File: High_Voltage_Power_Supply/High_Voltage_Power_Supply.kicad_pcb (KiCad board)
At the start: 2 copper layers, 170 x 100 mm, 64 parts, among them J1 Conn_01x02_Female, J2 Conn_01x02_Female, J3 Conn_01x02_Female, J4 Conn_01x12_Female, Q1 Q_NMOS_GDS, Q2 Q_NMOS_GDS, Q3 Q_NIGBT_GCE, U1 LT3751-TSSOP, U2 LT3751-TSSOP, U3 MC14504B, U4 MC14504B, U5 ADCMP356, U6 ZXGD3004E6

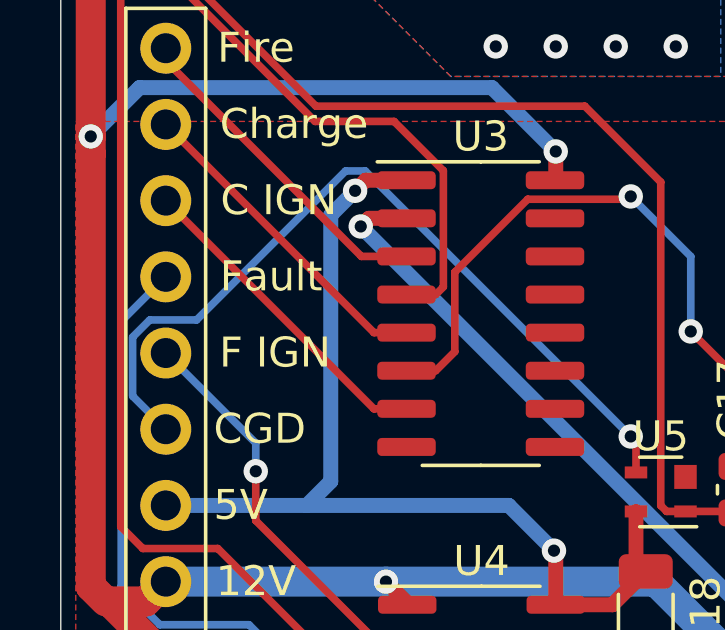
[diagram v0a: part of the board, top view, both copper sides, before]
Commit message: pin labling error fixed and arduino project for testing added
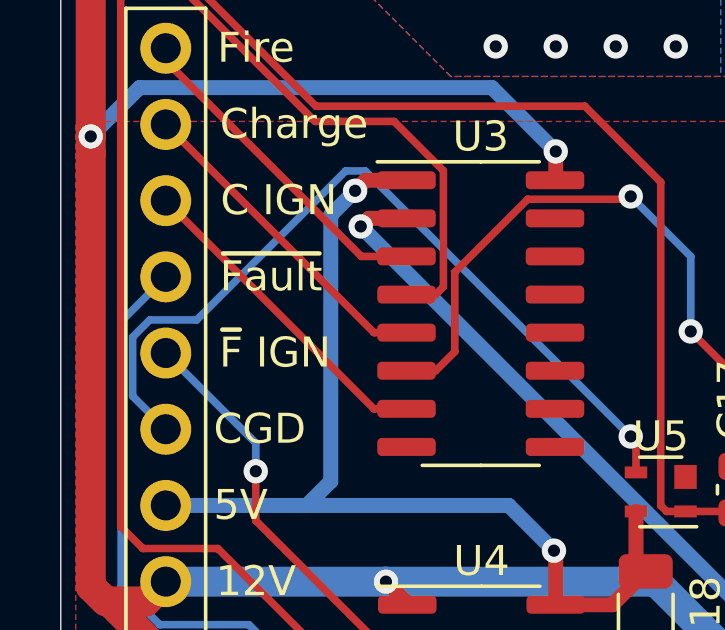
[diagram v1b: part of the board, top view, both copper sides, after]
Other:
- board text added: "~F IGN~"
- board text added: "~Fault~"
- board text removed: "F IGN"
- board text removed: "Fault"

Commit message: Created V3 of the schematic
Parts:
- added C19: 5uF, Capacitor_THT:C_Rect_L31.5mm_W20.0mm_P27.50mm_MKS4, F.Cu at (180.0, 130.0)
- added C20: 100uF, Capacitor_THT:CP_Radial_D8.0mm_P5.00mm, F.Cu at (70.0, 90.0)
- added C21: 100uF, Capacitor_THT:CP_Radial_D8.0mm_P5.00mm, F.Cu at (90.0, 135.0)
- added C22: 100uF, Capacitor_THT:CP_Radial_D8.0mm_P5.00mm, F.Cu at (70.0, 175.0)
- added C23: 10uF, Capacitor_SMD:C_1206_3216Metric, F.Cu at (182.5, 184.4)
- added C24: 10uF, Capacitor_SMD:C_1206_3216Metric, F.Cu at (167.3, 189.8)
- added C25: 10uF, Capacitor_SMD:C_1206_3216Metric, F.Cu at (182.5, 181.1)
- added C26: 10uF, Capacitor_SMD:C_1206_3216Metric, F.Cu at (167.2, 193.2)
- added C27: 10uF, Capacitor_SMD:C_1206_3216Metric, F.Cu at (141.8, 222.8)
- added C28: 10uF, Capacitor_SMD:C_1206_3216Metric, F.Cu at (145.9, 219.3)
- added C29: 10uF, Capacitor_SMD:C_1206_3216Metric, F.Cu at (164.0, 199.5)
- added C30: 10uF, Capacitor_SMD:C_1206_3216Metric, F.Cu at (176.3, 185.3)
- added C31: 10uF, Capacitor_SMD:C_1206_3216Metric, F.Cu at (173.0, 189.8)
- added C32: 10uF, Capacitor_SMD:C_1206_3216Metric, F.Cu at (136.1, 226.2)
- added C33: 10uF, Capacitor_SMD:C_1206_3216Metric, F.Cu at (155.6, 207.7)
- added C34: 2200pF, Capacitor_SMD:C_1812_4532Metric, F.Cu at (215.0, 65.0)
- added C35: 10nF, Capacitor_SMD:C_0603_1608Metric, F.Cu at (166.0, 205.8)
- added C36: 10nF, Capacitor_SMD:C_0603_1608Metric, F.Cu at (156.3, 213.9)
- added C37: 10nF, Capacitor_SMD:C_0603_1608Metric, F.Cu at (174.5, 196.1)
- added D3: B3100-13-F, Diode_SMD:D_SMC, F.Cu at (70.0, 165.0)
- added L1: 33uH, Inductor_SMD:L_Bourns_SRR1260, F.Cu at (69.8, 150.0)
- added Q4: Q_NIGBT_GCE, Package_TO_SOT_THT:TO-247-3_Vertical, F.Cu at (185.0, 115.0)
- added R29: 4m, Resistor_SMD:R_2512_6332Metric, F.Cu at (55.0, 93.0)
- added R30: 4m, Resistor_SMD:R_2512_6332Metric, F.Cu at (50.0, 93.0)
- added R31: 4m, Resistor_SMD:R_2512_6332Metric, F.Cu at (45.0, 93.0)
- added R32: 4m, Resistor_SMD:R_2512_6332Metric, F.Cu at (90.0, 148.0)
- added R33: 4m, Resistor_SMD:R_2512_6332Metric, F.Cu at (85.0, 148.0)
- added U10: ADR3412, Package_TO_SOT_SMD:SOT-23-6, F.Cu at (169.3, 200.5)
- added U11: LMR16030S, Package_SO:SOIC-8-1EP_3.9x4.9mm_P1.27mm_EP2.41x3.3mm_ThermalVias, F.Cu at (55.0, 155.0)
- added U7: LM7805, Package_TO_SOT_SMD:SOT-223-3_TabPin2, F.Cu at (71.8, 185.0)
- added U8: LM7805, Package_TO_SOT_SMD:SOT-223-3_TabPin2, F.Cu at (56.9, 185.0)
- added U9: LMV331, Package_TO_SOT_SMD:SOT-353_SC-70-5, F.Cu at (187.4, 183.7)
- C1: value 2200pF -> 1000uF; footprint Capacitor_SMD:C_1812_4532Metric -> Capacitor_THT:CP_Radial_D18.0mm_P7.50mm; moved to F.Cu
- C10, C9: value 1000uF -> 10uF; footprint Capacitor_THT:CP_Radial_D18.0mm_P7.50mm -> Capacitor_SMD:C_1210_3225Metric
- C11, C12: footprint Capacitor_SMD:C_1206_3216Metric -> Capacitor_SMD:C_1210_3225Metric
- C13: value 100uF -> 10uF; footprint Capacitor_THT:CP_Radial_D8.0mm_P5.00mm -> Capacitor_SMD:C_1210_3225Metric
- C14: value 100uF -> 150pF; footprint Capacitor_THT:CP_Radial_D8.0mm_P5.00mm -> Capacitor_SMD:C_1206_3216Metric
- C15: value 10nF -> 150pF; footprint Capacitor_SMD:C_0603_1608Metric -> Capacitor_SMD:C_1206_3216Metric; moved to F.Cu
- C16: value 10nF -> 0.1uF; footprint Capacitor_SMD:C_0603_1608Metric -> Capacitor_SMD:C_1206_3216Metric; moved to F.Cu
- C17: value 10nF -> 0.1uF; footprint Capacitor_SMD:C_0603_1608Metric -> Capacitor_SMD:C_1206_3216Metric
- C18: value 10uF -> 0.1uF
- C2: value 5uF -> 1000uF; footprint Capacitor_THT:C_Rect_L31.5mm_W20.0mm_P27.50mm_MKS4 -> Capacitor_THT:CP_Radial_D18.0mm_P7.50mm
- C3, C4, C5, C6: value 10uF -> 1000uF; footprint Capacitor_SMD:C_1210_3225Metric -> Capacitor_THT:CP_Radial_D18.0mm_P7.50mm; moved to F.Cu
- Q3: value Q_NIGBT_GCE -> Q_NMOS_GDS; footprint Package_TO_SOT_THT:TO-247-3_Vertical -> Package_TO_SOT_THT:TO-264-3_Vertical
- R1, R2, R3, R4, R5: value 4m -> 100k; footprint Resistor_SMD:R_2512_6332Metric -> Resistor_SMD:R_0603_1608Metric
- R10, R11: value 2.43k -> 4.87k; moved to F.Cu
- R12: value 4.87k -> 36.5k; footprint Resistor_SMD:R_1206_3216Metric -> Resistor_SMD:R_0603_1608Metric; moved to F.Cu
- R15: value 80.6k -> 1.3M; footprint Resistor_SMD:R_0603_1608Metric -> Resistor_SMD:R_0805_2012Metric; moved to F.Cu
- R16: value 80.6k -> 1.3M; footprint Resistor_SMD:R_0603_1608Metric -> Resistor_SMD:R_0805_2012Metric
- R17: value 453k -> 169k; moved to F.Cu
- R18: value 453k -> 169k
- R21: value 1.3M -> 453k; moved to F.Cu
- R22: value 1.3M -> 453k
- R23, R24: value 169k -> 80.6k; footprint Resistor_SMD:R_0805_2012Metric -> Resistor_SMD:R_0603_1608Metric
- R25, R26, R27: value 100k -> 4.7k; footprint Resistor_SMD:R_0603_1608Metric -> Resistor_SMD:R_1206_3216Metric
- R28: value 100k -> 4m; footprint Resistor_SMD:R_0603_1608Metric -> Resistor_SMD:R_2512_6332Metric
- R6: value 4m -> 2M; footprint Resistor_SMD:R_2512_6332Metric -> Resistor_SMD:R_1206_3216Metric
- R7, R8: moved to F.Cu
- R9: value 2M -> 4.87k; moved to F.Cu
- U3, U4: value MC14504B -> ZXGD3004E6; footprint Package_SO:SOIC-16_3.9x9.9mm_P1.27mm -> Package_TO_SOT_SMD:SOT-23-6
- U5: value ADCMP356 -> MC14504B; footprint Package_TO_SOT_SMD:Analog_KS-4 -> Package_SO:SOIC-16_3.9x9.9mm_P1.27mm
- U6: value ZXGD3004E6 -> MC14504B; footprint Package_TO_SOT_SMD:SOT-23-6 -> Package_SO:SOIC-16_3.9x9.9mm_P1.27mm; moved to F.Cu
- moved R7 168.8 mm to (136.1, 229.5), turned to 0 degrees
- moved R15 167.0 mm to (138.0, 232.6), turned to 0 degrees
- moved C1 163.9 mm to (50.0, 50.0)
- moved U6 158.7 mm to (35.0, 133.1)
- moved C15 155.8 mm to (110.2, 238.5), turned to 0 degrees
- moved R26 149.0 mm to (141.7, 226.2), turned to 0 degrees
- moved R8 144.1 mm to (151.5, 214.3), turned to 0 degrees
- moved R23 142.4 mm to (174.5, 198.6), turned to 0 degrees
- moved R21 139.4 mm to (117.6, 206.5), turned to 0 degrees
- moved C11 139.3 mm to (110.2, 234.7), turned to 0 degrees
- moved R13 138.7 mm to (140.9, 229.1), turned to 0 degrees
- moved C2 137.9 mm to (50.0, 70.0)
- moved R18 137.4 mm to (178.0, 191.8), turned to 0 degrees
- moved R17 136.0 mm to (187.5, 180.2), turned to 0 degrees
- moved C9 133.5 mm to (145.9, 215.5)
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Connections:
- C1 pad 1: Net-(C1-Pad1) -> Vtrans
- C11 pad 1: VCC -> Vtrans
- C12 pad 1: VCC -> Vtrans
- C13 pad 1: VCC -> Vtrans
- C14 pad 1: VCC -> Net-(C14-Pad1)
- C14 pad 2: GND -> /Transformer/in-
- C15 pad 2: GND -> Net-(C15-Pad2)
- C16 pad 2: GND -> Net-(C16-Pad2)
- C17 pad 1: Net-(C17-Pad1) -> +5VA
- C18 pad 1: +5V -> Net-(C18-Pad1)
- C2 pad 1: Net-(C2-Pad1) -> Vtrans
- D1 pad 1: Net-(C1-Pad1) -> Net-(C34-Pad1)
- D2 pad 1: Net-(C2-Pad1) -> Net-(C19-Pad1)
- J2 pad 2: Net-(C1-Pad1) -> Net-(C34-Pad1)
- J3 pad 2: Net-(C2-Pad1) -> Net-(C19-Pad1)
- J4 pad 5: VCC -> +5VD
- J4 pad 6: +5V -> +5VD
- Q1 pad 1: Net-(Q1-Pad1) -> Drive_out
- Q2 pad 1: Net-(Q2-Pad1) -> Drive_out
- Q2 pad 2: Net-(Q2-Pad2) -> /Transformer/in-
- Q2 pad 3: Net-(Q2-Pad3) -> Net-(Q1-Pad3)
- Q3 pad 2: Net-(J3-Pad1) -> Net-(C15-Pad2)
- Q3 pad 3: GND -> Net-(Q3-Pad3)
- R1 pad 1: Net-(Q1-Pad3) -> Net-(R1-Pad1)
- R1 pad 2: GND -> VCC
- R10 pad 1: Net-(C15-Pad1) -> Net-(C36-Pad1)
- R10 pad 2: Net-(C17-Pad1) -> GND
- R11 pad 1: Net-(C17-Pad1) -> Net-(R11-Pad1)
- R12 pad 1: Net-(C16-Pad1) -> /Transformer/in-
- R12 pad 2: GND -> Net-(R12-Pad2)
- R13 pad 1: /Transformer/in- -> Net-(C15-Pad2)
- R14 pad 1: Net-(Q2-Pad2) -> GND
- R15 pad 1: Vtrans -> Net-(R15-Pad1)
- R15 pad 2: Net-(R15-Pad2) -> Vtrans
- R16 pad 1: Vtrans -> Net-(R16-Pad1)
- R16 pad 2: Net-(R16-Pad2) -> Vtrans
- R17 pad 2: Vtrans -> VCC
- R2 pad 1: Net-(Q1-Pad3) -> ~FAULT~
- R2 pad 2: GND -> VCC
- R22 pad 2: Vtrans -> VCC
- R23 pad 1: Net-(R23-Pad1) -> Vtrans
- R23 pad 2: VCC -> Net-(R23-Pad2)
- R24 pad 1: Net-(R24-Pad1) -> Vtrans
- R24 pad 2: VCC -> Net-(R24-Pad2)
- R25 pad 1: Net-(R25-Pad1) -> Vtrans
- R25 pad 2: VCC -> Net-(C14-Pad1)
- R26 pad 1: ~FAULT~ -> Vtrans
- R26 pad 2: VCC -> Net-(C15-Pad1)
- R27 pad 1: Net-(R27-Pad1) -> +5VD
- R27 pad 2: VCC -> Charged
- R28 pad 1: ~FAULT_IGN~ -> Net-(Q1-Pad3)
- R28 pad 2: VCC -> GND
- R3 pad 1: Net-(Q1-Pad3) -> Net-(R3-Pad1)
- R3 pad 2: GND -> VCC
- R4 pad 1: Net-(Q1-Pad3) -> ~FAULT_IGN~
- R4 pad 2: GND -> VCC
- R5 pad 1: Net-(Q2-Pad3) -> Net-(R11-Pad1)
- R5 pad 2: GND -> VCC
- R6 pad 1: Net-(Q2-Pad3) -> Net-(C34-Pad1)
- R6 pad 2: GND -> Net-(R6-Pad2)
- R7 pad 1: Net-(C1-Pad1) -> Net-(R6-Pad2)
- R7 pad 2: Net-(R7-Pad2) -> Net-(C35-Pad1)
- R8 pad 1: Net-(R7-Pad2) -> Net-(C19-Pad1)
- R8 pad 2: Net-(C15-Pad1) -> Net-(C36-Pad1)
- R9 pad 1: Net-(C2-Pad1) -> Net-(C35-Pad1)
- R9 pad 2: Net-(C16-Pad1) -> GND
- TR3 pad 1: Net-(Q2-Pad2) -> Net-(C15-Pad2)
- TR3 pad 2: Net-(Q2-Pad2) -> Net-(C15-Pad2)
- TR3 pad 3: Net-(Q2-Pad2) -> Net-(C15-Pad2)
- TR3 pad 4: Net-(Q2-Pad2) -> Net-(C15-Pad2)
- U1 pad 1: Net-(R15-Pad2) -> Net-(R23-Pad2)
- U1 pad 10: Net-(C15-Pad1) -> Net-(C35-Pad1)
- U1 pad 15: Net-(Q1-Pad1) -> Drive_in
- U1 pad 2: Net-(R17-Pad1) -> Net-(R19-Pad1)
- U1 pad 20: Net-(R13-Pad2) -> Net-(R12-Pad2)
- U1 pad 3: Net-(R21-Pad1) -> Net-(R15-Pad1)
- U1 pad 4: Net-(R23-Pad1) -> Net-(R17-Pad1)
- U1 pad 5: Net-(R18-Pad1) -> Net-(R20-Pad1)
- U1 pad 7: Net-(R25-Pad1) -> Net-(R1-Pad1)
- U2 pad 1: Net-(R16-Pad2) -> Net-(R24-Pad2)
- U2 pad 10: Net-(C16-Pad1) -> Net-(C36-Pad1)
- U2 pad 12: Net-(Q2-Pad3) -> Net-(Q3-Pad3)
- U2 pad 15: Net-(Q2-Pad1) -> Net-(Q3-Pad1)
- U2 pad 2: Net-(R19-Pad1) -> Net-(R21-Pad1)
- U2 pad 20: Net-(R14-Pad2) -> Net-(R13-Pad2)
- U2 pad 3: Net-(R22-Pad1) -> Net-(R16-Pad1)
- U2 pad 4: Net-(R24-Pad1) -> Net-(R18-Pad1)
- U2 pad 5: Net-(R20-Pad1) -> Net-(R22-Pad1)
- U2 pad 7: Net-(R27-Pad1) -> Net-(R3-Pad1)
- U3 pad 1: +5V -> VCC
- U3 pad 2: FIRE -> Drive_in
- U3 pad 3: FIRE_5V -> GND
- U3 pad 4: CHARGE -> Drive_out
- U3 pad 5: CHARGE_5V -> Drive_in
- U3 pad 6: CHARGE_IGN -> Drive_out
- U4 pad 2: ~FAULT_IGN_5V~ -> FIRE
- U4 pad 3: ~FAULT~ -> GND
- U4 pad 4: ~FAULT_5V~ -> Net-(Q4-Pad1)
- U4 pad 5: ~FAULT_IGN~ -> FIRE
- U4 pad 6: Net-(U4-Pad6) -> Net-(Q4-Pad1)
- U5 pad 1: Net-(C17-Pad1) -> +5V
- U5 pad 2: GND -> FIRE
- U5 pad 3: Charged -> FIRE_5V
- U5 pad 4: +5V -> CHARGE
- U6 pad 2: FIRE -> ~FAULT_IGN_5V~
- U6 pad 3: GND -> ~FAULT~
- U6 pad 4: Net-(Q3-Pad1) -> ~FAULT_5V~
- U6 pad 5: FIRE -> ~FAULT_IGN~
- U6 pad 6: Net-(Q3-Pad1) -> Net-(U6-Pad6)
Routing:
- net VCC: track 291.3 -> 0.00 mm, vias 20 -> 0
- net FIRE: track 145.2 -> 0.00 mm, vias 1 -> 0
- net Net-(C17-Pad1): track 126.1 -> 0.00 mm, vias 1 -> 0
- net ~FAULT~: track 119.2 -> 0.00 mm
- net Net-(C15-Pad1): track 104.7 -> 0.00 mm, vias 1 -> 0
- net CHARGE: track 103.2 -> 0.00 mm
- net Net-(C16-Pad1): track 77.0 -> 0.00 mm, vias 1 -> 0
- net ~FAULT_IGN~: track 52.2 -> 0.00 mm, vias 4 -> 0
- net CHARGE_IGN: track 47.7 -> 0.00 mm, vias 2 -> 0
- net +5V: track 34.0 -> 0.00 mm, vias 2 -> 0
- net Net-(R14-Pad2): track 33.9 -> 0.00 mm
- net Net-(Q2-Pad3): track 33.1 -> 0.00 mm
- net Net-(Q2-Pad1): track 29.5 -> 0.00 mm
- net Charged: track 27.4 -> 0.00 mm, vias 1 -> 0
- net GND: track 27.2 -> 0.00 mm, vias 438 -> 0
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- removed copper zone on F.Cu, net /Transformer/in-
- removed copper zone on B.Cu, net /Transformer/out+
- removed copper zone on F.Cu, net /Transformer/out+
- removed copper zone on B.Cu, net GND
- removed copper zone on F.Cu, net GND
- removed copper zone on B.Cu, net Net-(C1-Pad1)
- removed copper zone on F.Cu, net Net-(C1-Pad1)
- removed copper zone on B.Cu, net Net-(C17-Pad1)
- removed copper zone on B.Cu, net Net-(C2-Pad1)
- removed copper zone on F.Cu, net Net-(C2-Pad1)
- removed copper zone on B.Cu, net Net-(D2-Pad2)
- removed copper zone on F.Cu, net Net-(D2-Pad2)
- removed copper zone on B.Cu, net Net-(J3-Pad1)
- removed copper zone on F.Cu, net Net-(J3-Pad1)
- removed copper zone on F.Cu, net Net-(Q1-Pad3)
- removed copper zone on F.Cu, net Net-(Q2-Pad2)
- removed copper zone on F.Cu, net Net-(Q2-Pad3)
- removed copper zone on B.Cu, net Net-(R7-Pad2)
- removed copper zone on B.Cu, net VCC
- removed copper zone on F.Cu, net VCC
- removed copper zone on B.Cu, net Vtrans
- removed copper zone on F.Cu, net Vtrans
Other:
- board outline removed
- board text removed: "12V"
- board text removed: "1kV"
- board text removed: "48V"
- board text removed: "5V"
- board text removed: "C IGN"
- board text removed: "CGD"
- board text removed: "Charge"
- board text removed: "Corwin Hansen corwinh.com/git akerunakayama@gmail.com (206) 462 8204"
- board text removed: "Fire"
- board text removed: "GND"
- board text removed: "IGN+"
- board text removed: "IGN-"
- board text removed: "~F IGN~"
- board text removed: "~Fault~"

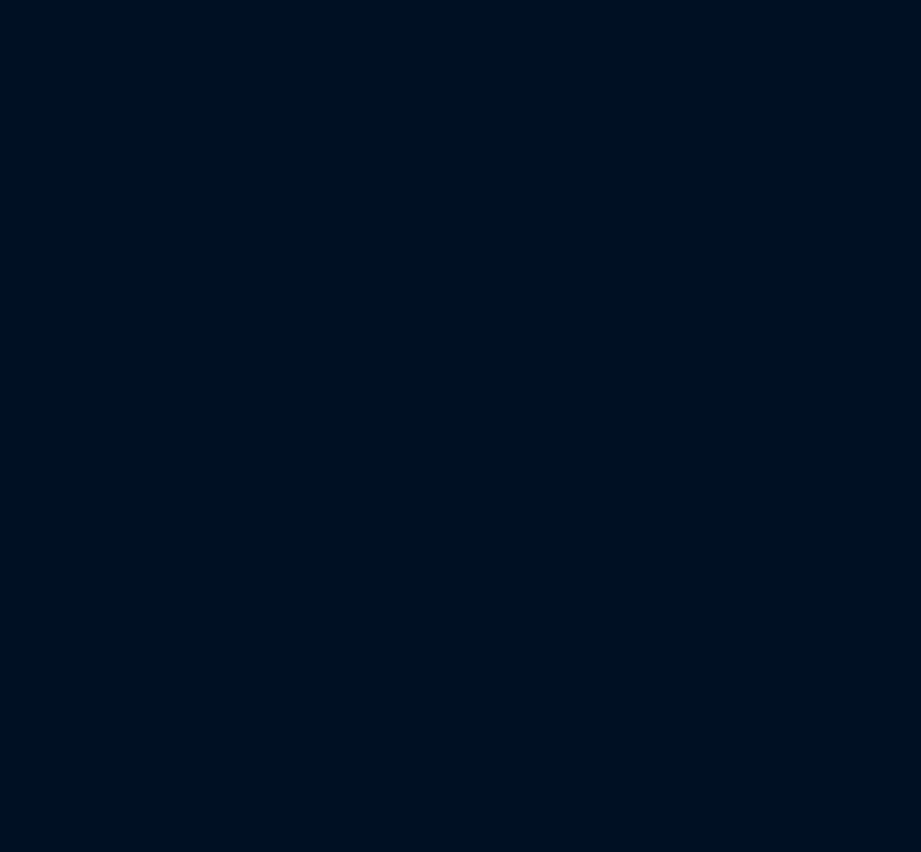
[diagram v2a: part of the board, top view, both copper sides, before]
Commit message: schematic update with mounting holes
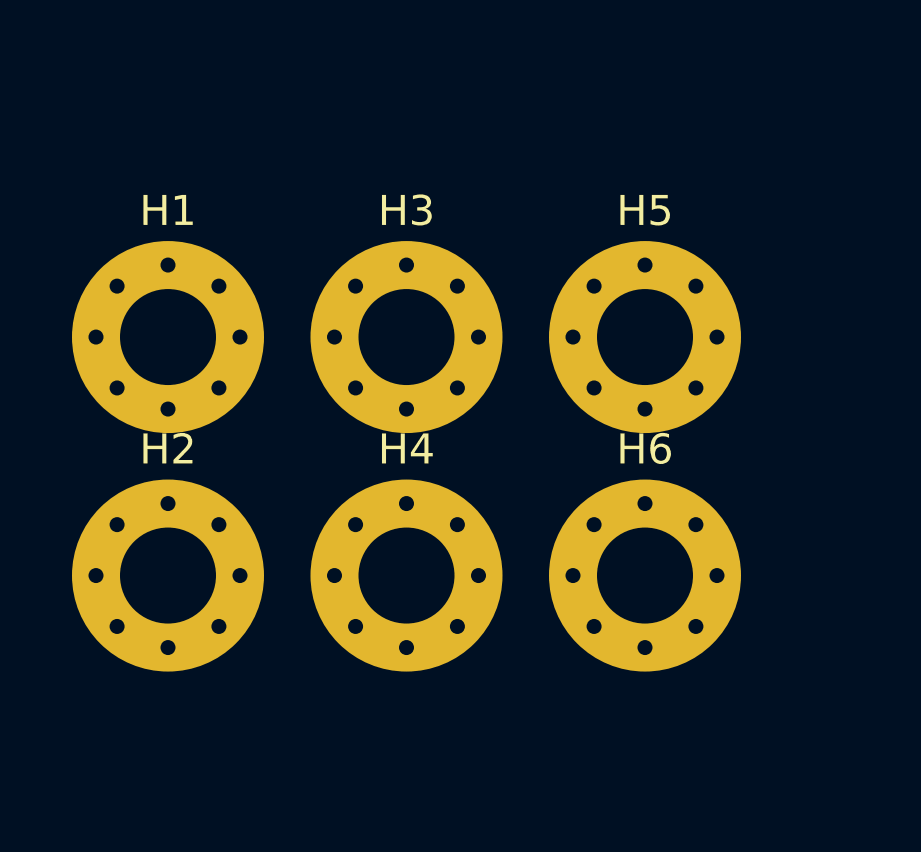
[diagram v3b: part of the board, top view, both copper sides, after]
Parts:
- added H1: MountingHole_Pad, MountingHole:MountingHole_3.2mm_M3_Pad_Via, F.Cu at (20.0, 170.0)
- added H2: MountingHole_Pad, MountingHole:MountingHole_3.2mm_M3_Pad_Via, F.Cu at (20.0, 177.9)
- added H3: MountingHole_Pad, MountingHole:MountingHole_3.2mm_M3_Pad_Via, F.Cu at (27.9, 170.0)
- added H4: MountingHole_Pad, MountingHole:MountingHole_3.2mm_M3_Pad_Via, F.Cu at (27.9, 177.9)
- added H5: MountingHole_Pad, MountingHole:MountingHole_3.2mm_M3_Pad_Via, F.Cu at (35.9, 170.0)
- added H6: MountingHole_Pad, MountingHole:MountingHole_3.2mm_M3_Pad_Via, F.Cu at (35.9, 177.9)

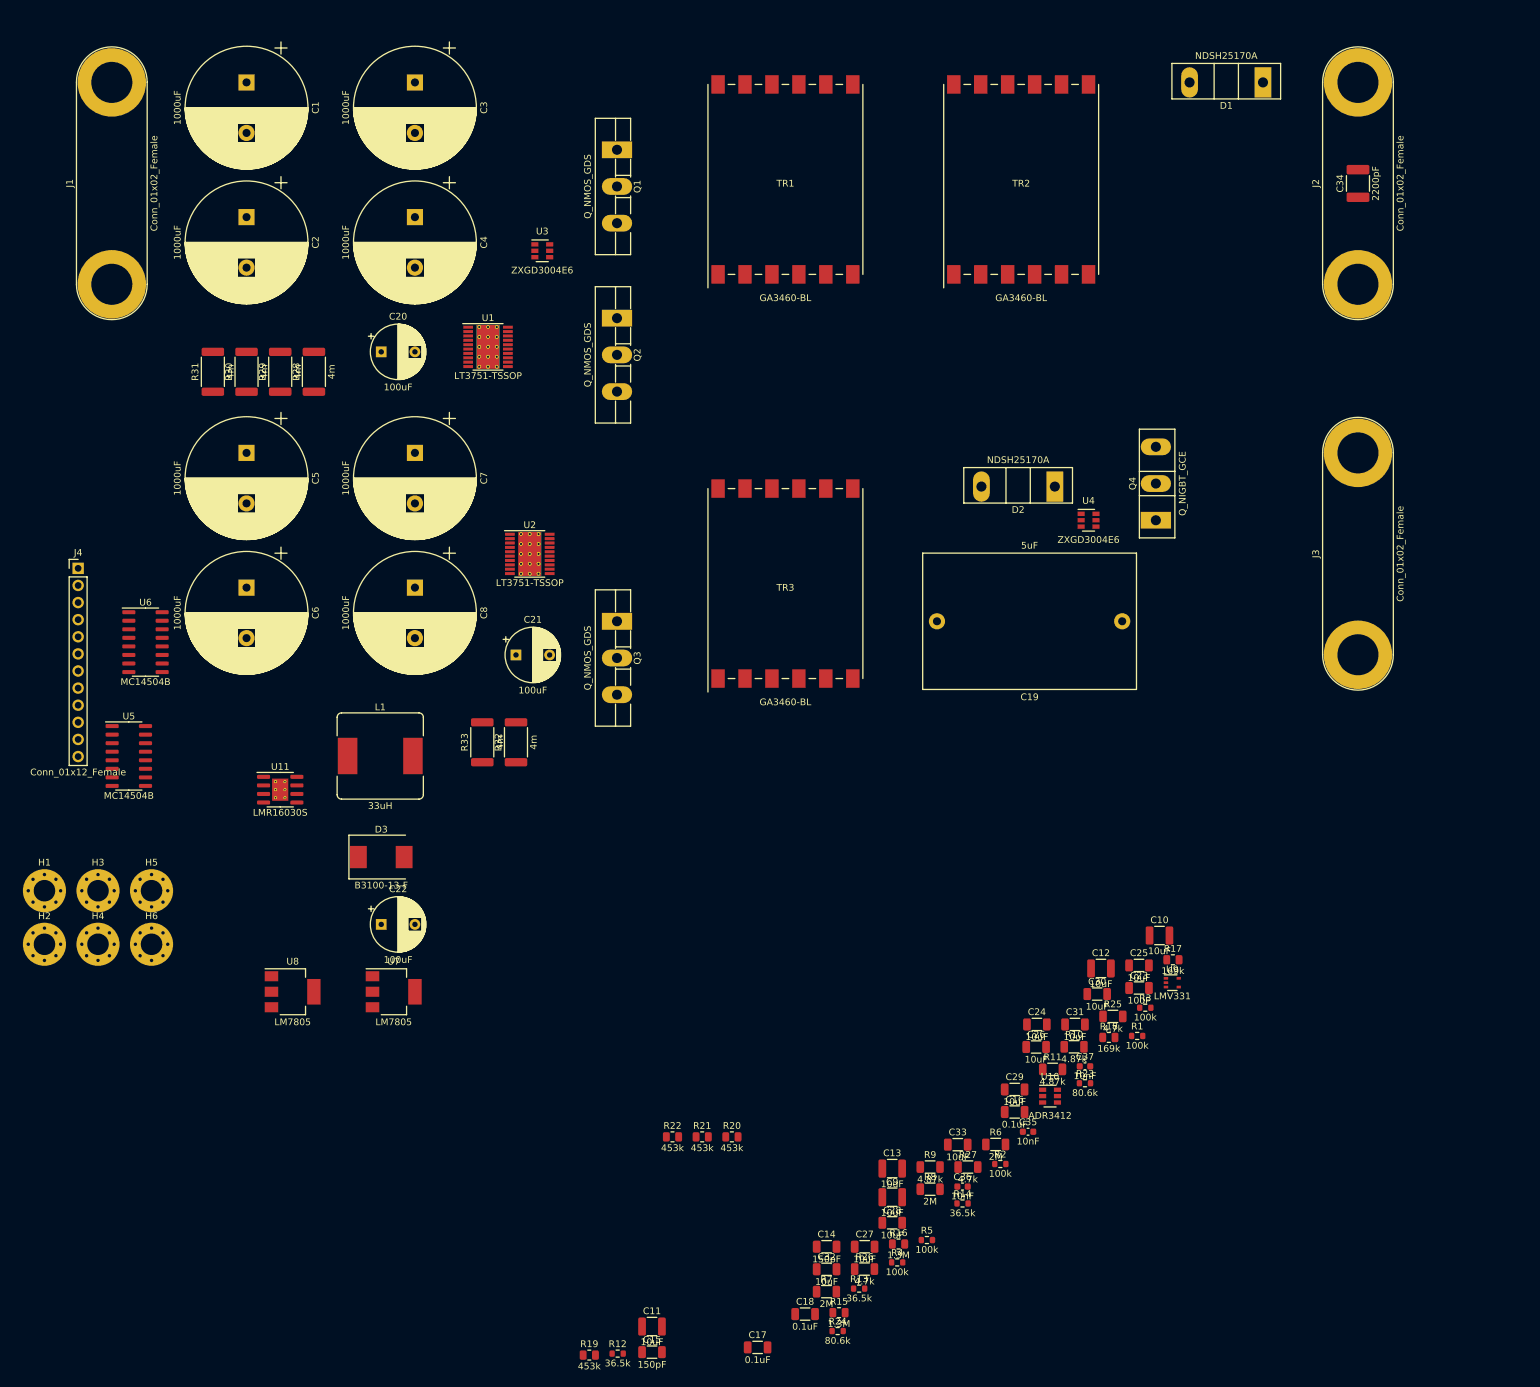
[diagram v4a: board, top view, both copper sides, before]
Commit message: Edited schematic to use new buck converter chip.
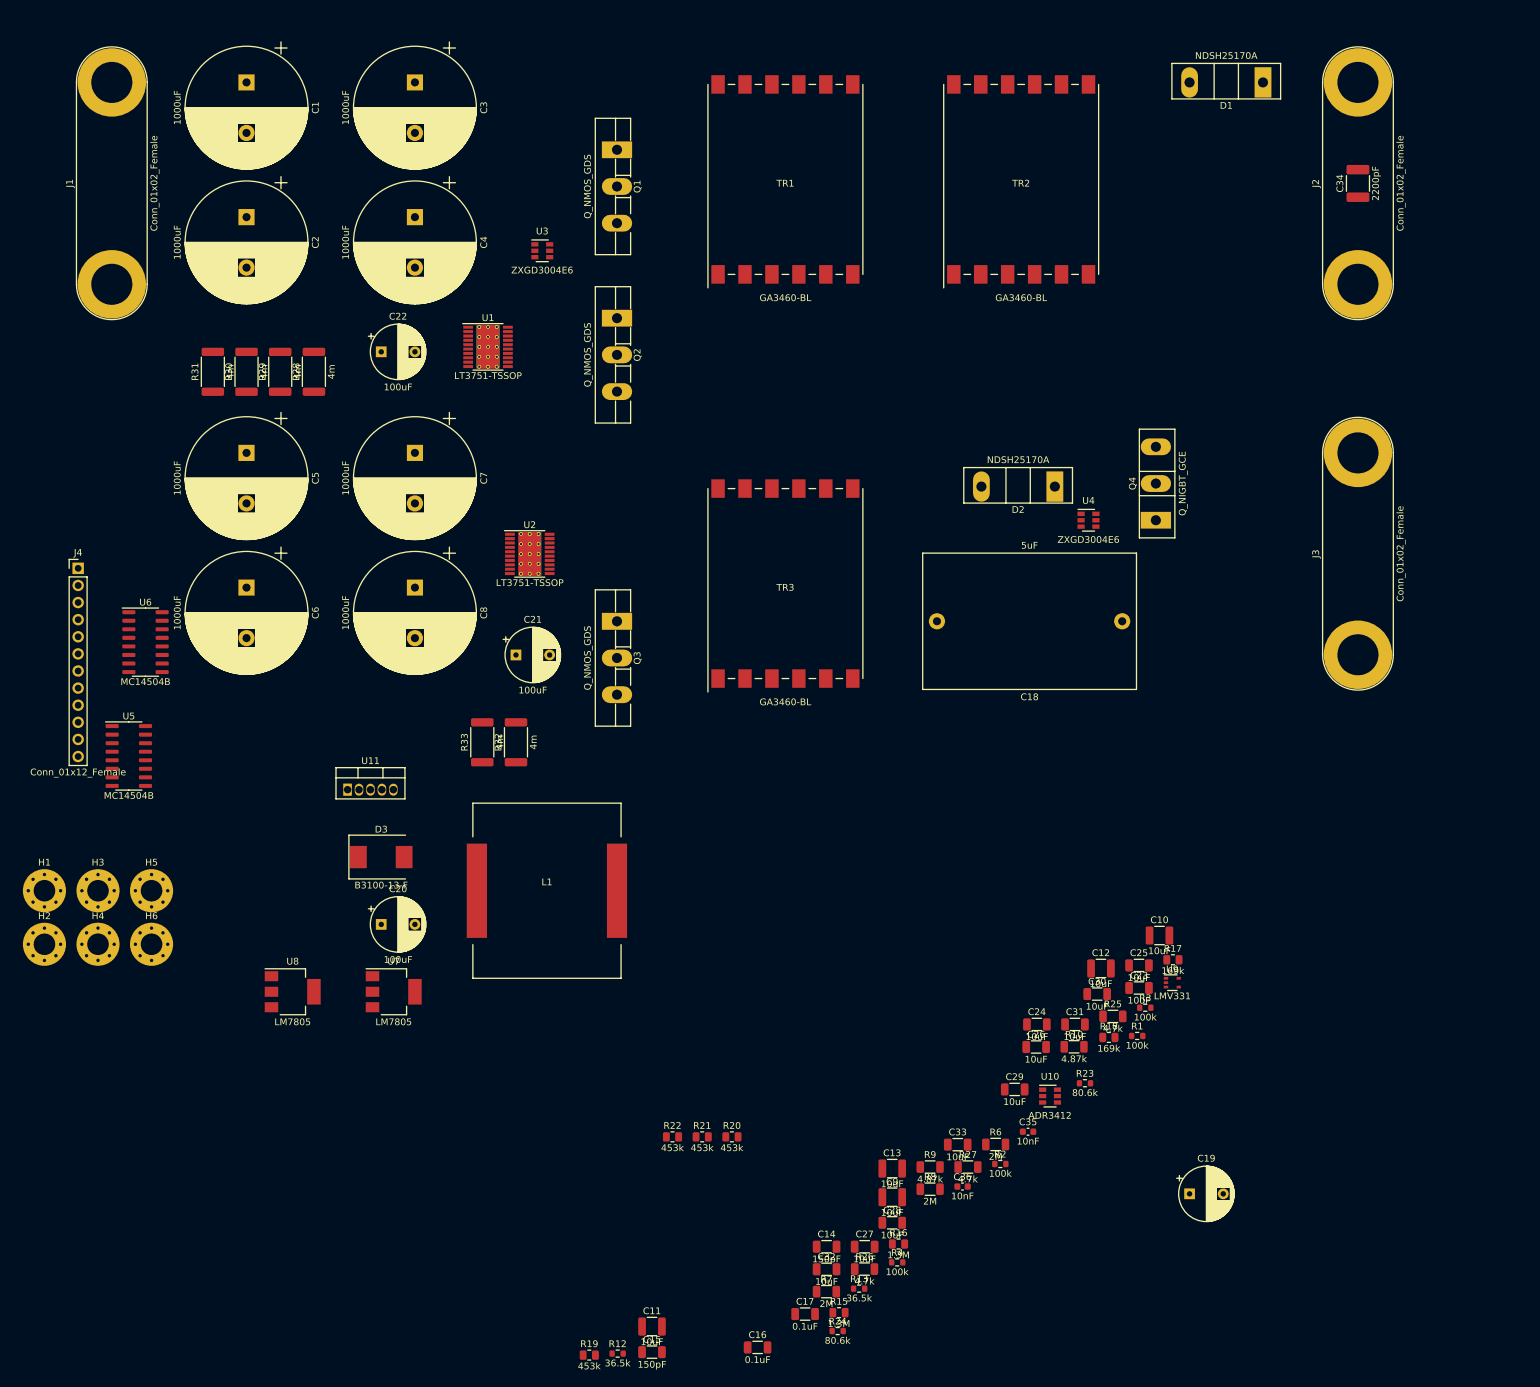
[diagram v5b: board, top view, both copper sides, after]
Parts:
- removed the C16 at (164.0, 202.8)
- removed C37: 10nF, Capacitor_SMD:C_0603_1608Metric
- removed R11: 4.87k, Resistor_SMD:R_1206_3216Metric
- removed R14: 36.5k, Resistor_SMD:R_0603_1608Metric
- removed R5: 100k, Resistor_SMD:R_0603_1608Metric
- added C19: 100uF, Capacitor_THT:CP_Radial_D8.0mm_P5.00mm, F.Cu at (190.0, 215.0)
- L1: value 33uH -> 330uH; footprint Inductor_SMD:L_Bourns_SRR1260 -> High_Voltage_Power_Supply:60B334C
- U11: value LMR16030S -> LM2576HVT-15; footprint Package_SO:SOIC-8-1EP_3.9x4.9mm_P1.27mm_EP2.41x3.3mm_ThermalVias -> Package_TO_SOT_THT:TO-220-5_Vertical
- moved L1 31.8 mm to (94.6, 170.0)
- moved U11 10.0 mm to (65.0, 155.0)
- renumbered C17 to C16, C18 to C17, C19 to C18, C22 to C20, C20 to C22
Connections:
- D3 pad 1: Net-(C16-Pad2) -> Net-(D3-Pad1)
- L1 pad 1: Net-(C16-Pad2) -> Net-(D3-Pad1)
- U11 pad 1: Net-(C16-Pad1) -> Vtrans
- U11 pad 2: Vtrans -> Net-(D3-Pad1)
- U11 pad 3: Vtrans -> GND
- U11 pad 4: Net-(R14-Pad2) -> VCC
- U11 pad 5: Net-(R11-Pad1) -> GND
